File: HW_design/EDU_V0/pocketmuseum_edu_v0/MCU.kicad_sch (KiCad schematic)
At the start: 31 parts, among them J201 DM3AT-SF-PEJM5, J204 BM04B-SRSS-TB, J205 BM04B-SRSS-TB, J206 BM04B-SRSS-TB, SW201 PTS636, U201 ESP32-C6-MINI-1/U

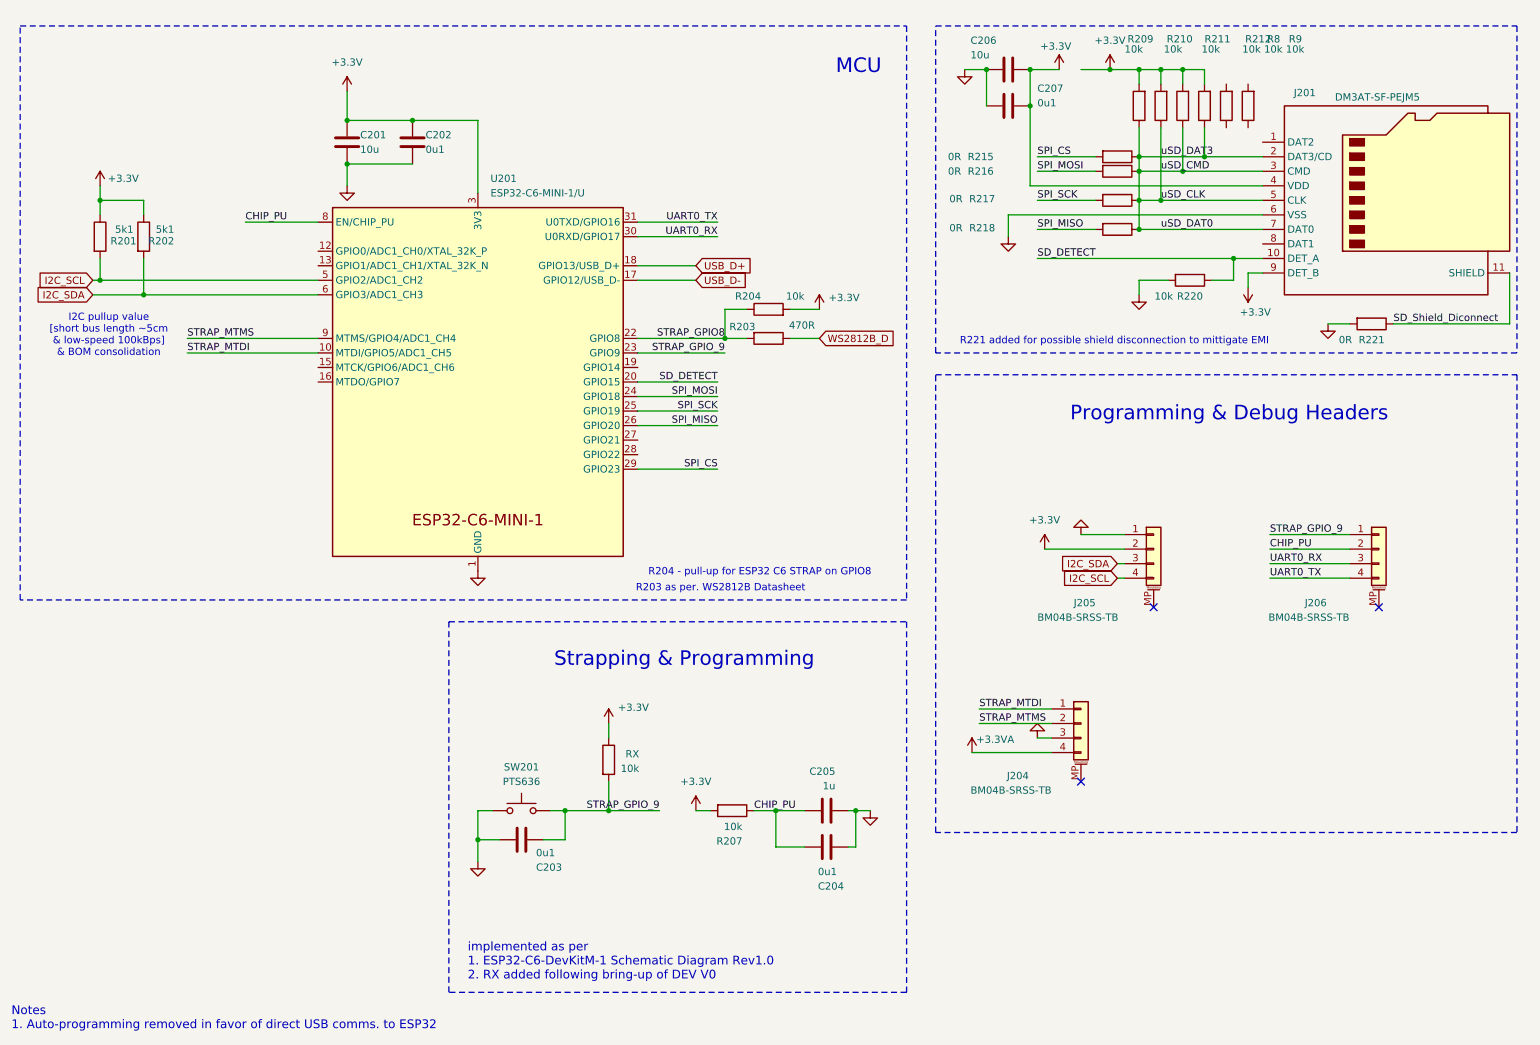
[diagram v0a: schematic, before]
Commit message: [EDUV0] Cleaned-up uSD card
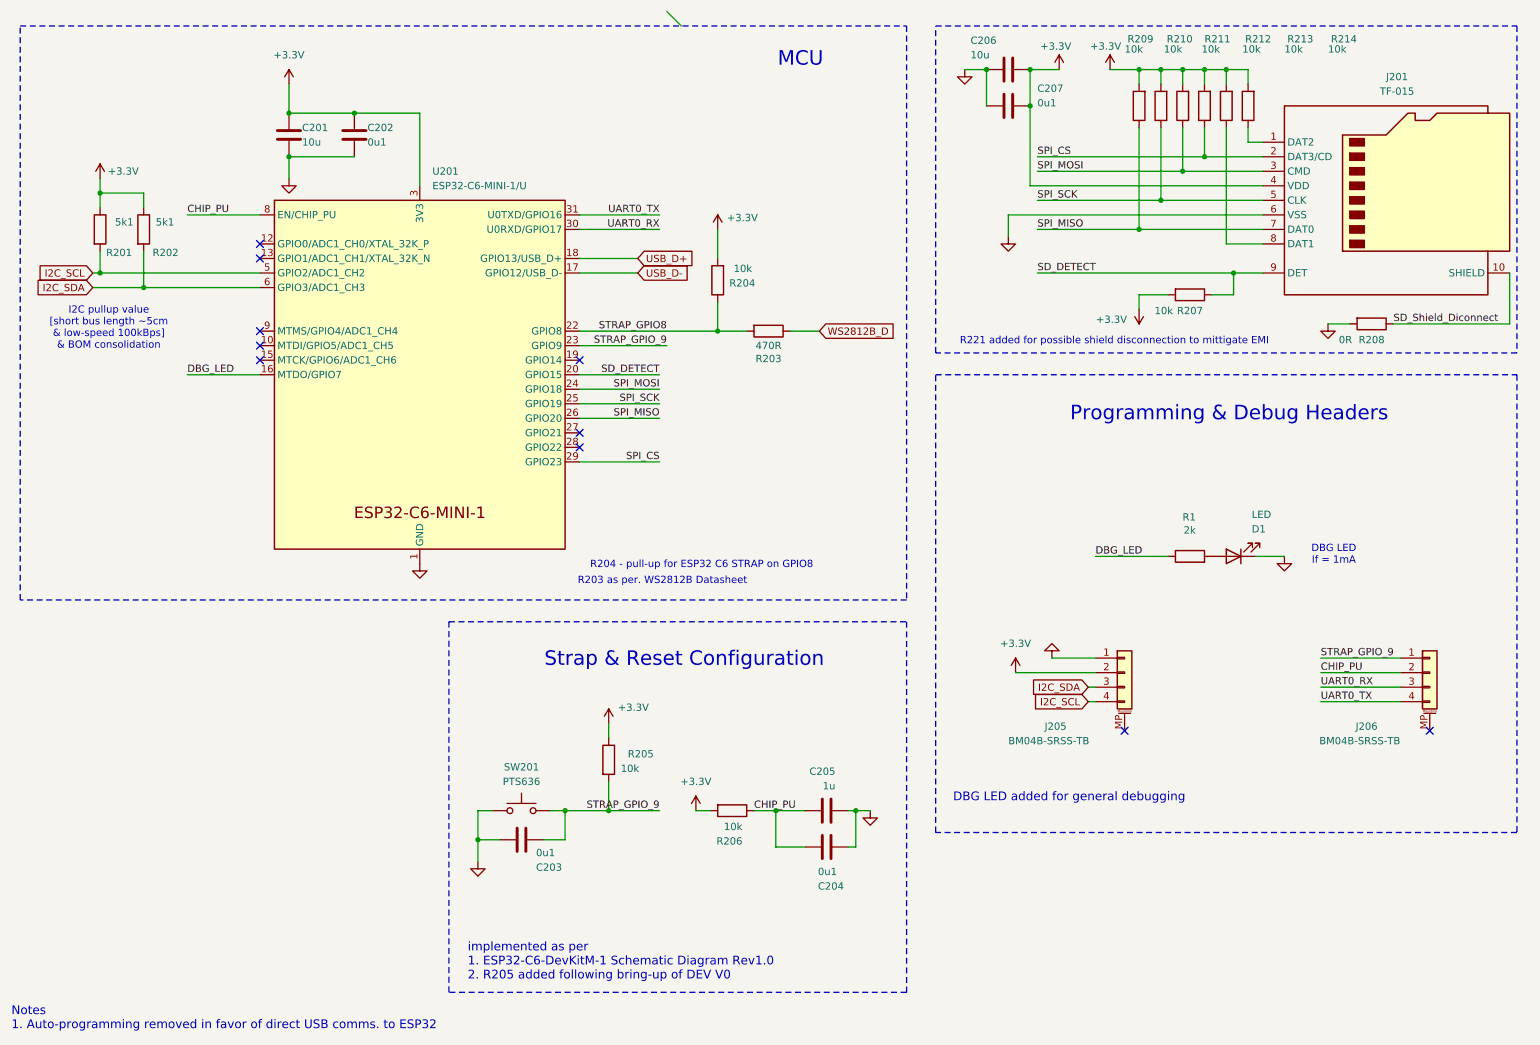
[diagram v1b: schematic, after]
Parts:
- removed J201: DM3AT-SF-PEJM5, Connector_Card:microSD_HC_Hirose_DM3AT-SF-PEJM5, symbol Connector:Micro_SD_Card_Det2
- removed J204: BM04B-SRSS-TB, Connector_JST:JST_SH_BM04B-SRSS-TB_1x04-1MP_P1.00mm_Vertical, symbol Connector_Generic_MountingPin:Conn_01x04_MountingPin
- removed R215, R216, R217, R218: 0R, Resistor_SMD:R_0603_1608Metric, symbol Device:R
- added D1: LED, LED_SMD:LED_0402_1005Metric, symbol Device:LED
- added J201: TF-015, microSD:TF-015_SOFNG, symbol Connector:Micro_SD_Card_Det1
- added R1: 2k, Resistor_SMD:R_0402_1005Metric, symbol Device:R
- renumbered RX to R205, R207 to R206, R220 to R207, R221 to R208, R8 to R213, R9 to R214
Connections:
- net +3.3V: now also R207.2, R213.2, R214.2, J201.4 (VDD)
- net GND: now also D1.1 (K), J201.6 (VSS); no longer R207.2
- net SD_DETECT: now also J201.9 (DET)
- net SD_Shield_Diconnect: now also J201.10 (SHIELD)
- net SPI_CS: now also R212.1, J201.2 (DAT3/CD)
- net SPI_MISO: now also R209.1, J201.7 (DAT0)
- net SPI_MOSI: now also R211.1, J201.3 (CMD)
- net SPI_SCK: now also R210.1, J201.5 (CLK)
- net at R214.1: now also J201.1 (DAT2)
- net at R213.1: now also J201.8 (DAT1)
- net DBG_LED: now reaches U201.16 (MTDO/GPIO7)
- net DBG_LED: now also R1.1
- net STRAP_MTDI: no longer names the net of U201.10 (MTDI/GPIO5/ADC1_CH5)
- net STRAP_MTMS: no longer names the net of U201.9 (MTMS/GPIO4/ADC1_CH4)
- removed net uSD_CLK: R209.1, R210.1, R211.1, R212.1
- new net: D1.2 (A), R1.2
- no-connect marks 3 -> 10
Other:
- note added: "DBG LED If = 1mA"
- note added: "DBG LED added for general debugging"
- note added: "Strap & Reset Configuration"
- note added: "implemented as per 1. ESP32-C6-DevKitM-1 Schematic Diagram Rev1.0 2. R205 added following bring-up of DEV V0"
- note removed: "Strapping & Programming"
- note removed: "implemented as per 1. ESP32-C6-DevKitM-1 Schematic Diagram Rev1.0 2. RX added following bring-up of DEV V0"
- moved on the sheet: C201, C202, J205, J206, R201, R202, R203, R204, R207, U201
